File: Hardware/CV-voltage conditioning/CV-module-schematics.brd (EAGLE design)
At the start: 72.4 x 100 mm, 62 parts, among them IC2 LM358D, IC3 LM358D, IC4 LM358D, IC5 LM358D

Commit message: updates
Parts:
- added JP3: (no value), pinhead:1X03
- moved JP2 169.2 mm to (17.8, 92.7), turned to 90 degrees
- moved JP1 83.5 mm to (20.3, 14.0), turned to 180 degrees
- moved C7 81.2 mm to (16.5, 22.9), flipped to the bottom
- moved C3 80.8 mm to (-8.89, 38.1)
- moved C8 80.7 mm to (12.7, 19.1)
- moved C4 76.9 mm to (-7.62, 30.5)
- moved C5 66.5 mm to (29.2, 11.4)
- moved C1 59.5 mm to (-8.89, 24.1)
- moved C6 58.5 mm to (15.2, 3.81), flipped to the bottom, turned to 90 degrees
- moved R7 48.7 mm to (17.7, 19.6), flipped to the bottom, turned to 90 degrees
- moved C2 47.9 mm to (27.9, 2.54), flipped to the bottom, turned to 270 degrees
- moved R5 42.6 mm to (20.4, 19.6), flipped to the bottom, turned to 90 degrees
- moved R8 41.0 mm to (17.8, 7.62), turned to 270 degrees
- moved R3 37.1 mm to (22.8, 19.7), flipped to the bottom, turned to 90 degrees
- moved R6 35.3 mm to (20.3, 7.62), flipped to the bottom, turned to 270 degrees
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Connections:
- net +12VDC: now also JP3.1
- net -12VDC: now also JP3.3
- net GND: now also JP3.2
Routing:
- net N$28: track 0.00 -> 105.0 mm, vias 0 -> 1
- net N$32: track 0.00 -> 82.4 mm, vias 0 -> 1
- net N$1: track 0.00 -> 72.4 mm, vias 0 -> 1
- net N$3: track 0.00 -> 71.1 mm
- net N$30: track 0.00 -> 68.8 mm
- net N$2: track 0.00 -> 67.3 mm
- net N$31: track 0.00 -> 59.5 mm, vias 0 -> 2
- net N$29: track 0.00 -> 34.1 mm, vias 0 -> 2
- net +5V: track 192.0 -> 183.0 mm
- net -12VDC: track 160.7 -> 168.9 mm
- net GND: track 193.3 -> 200.2 mm, vias 5 -> 4
- net +12VDC: track 211.6 -> 216.8 mm
- net VDAC4: track 0.00 -> 4.27 mm
- net VDAC8: track 0.00 -> 4.23 mm
- net VDAC6: track 0.00 -> 4.23 mm
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
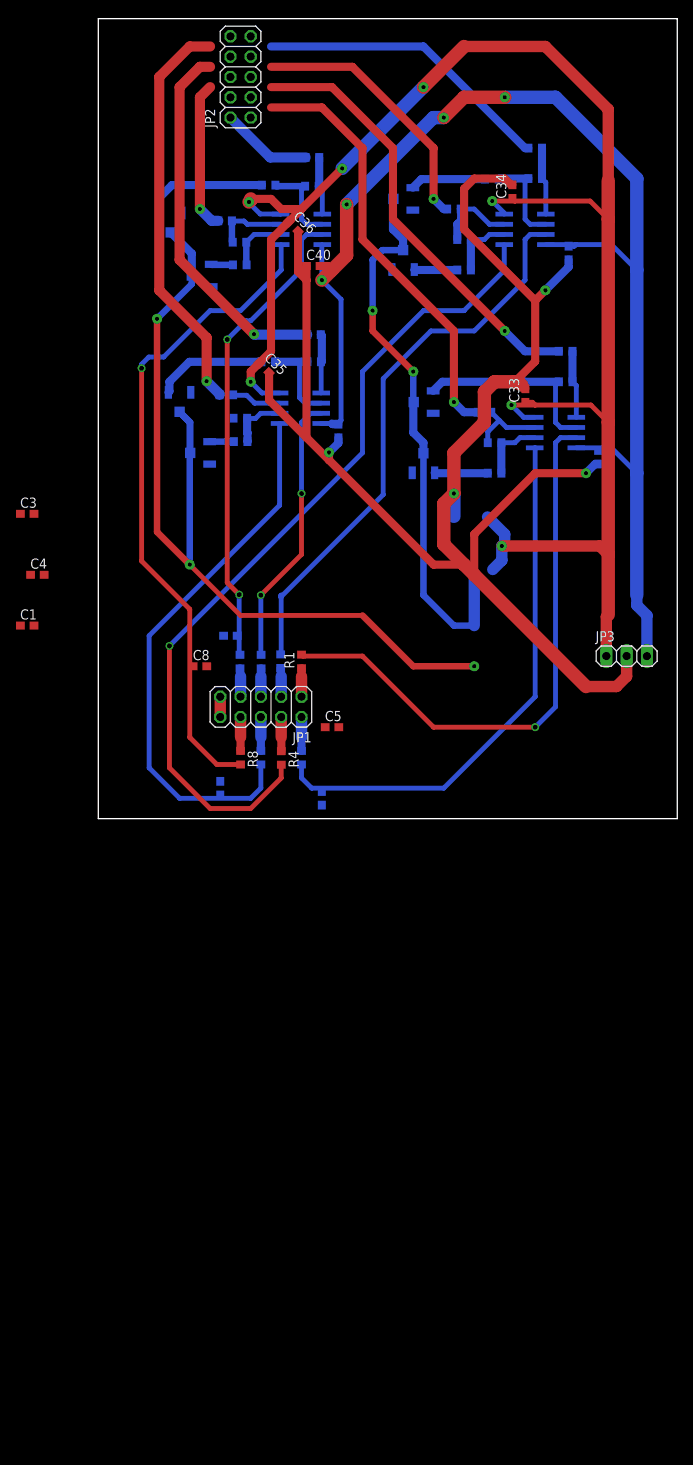
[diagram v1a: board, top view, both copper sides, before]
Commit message: updates for voltage-level module
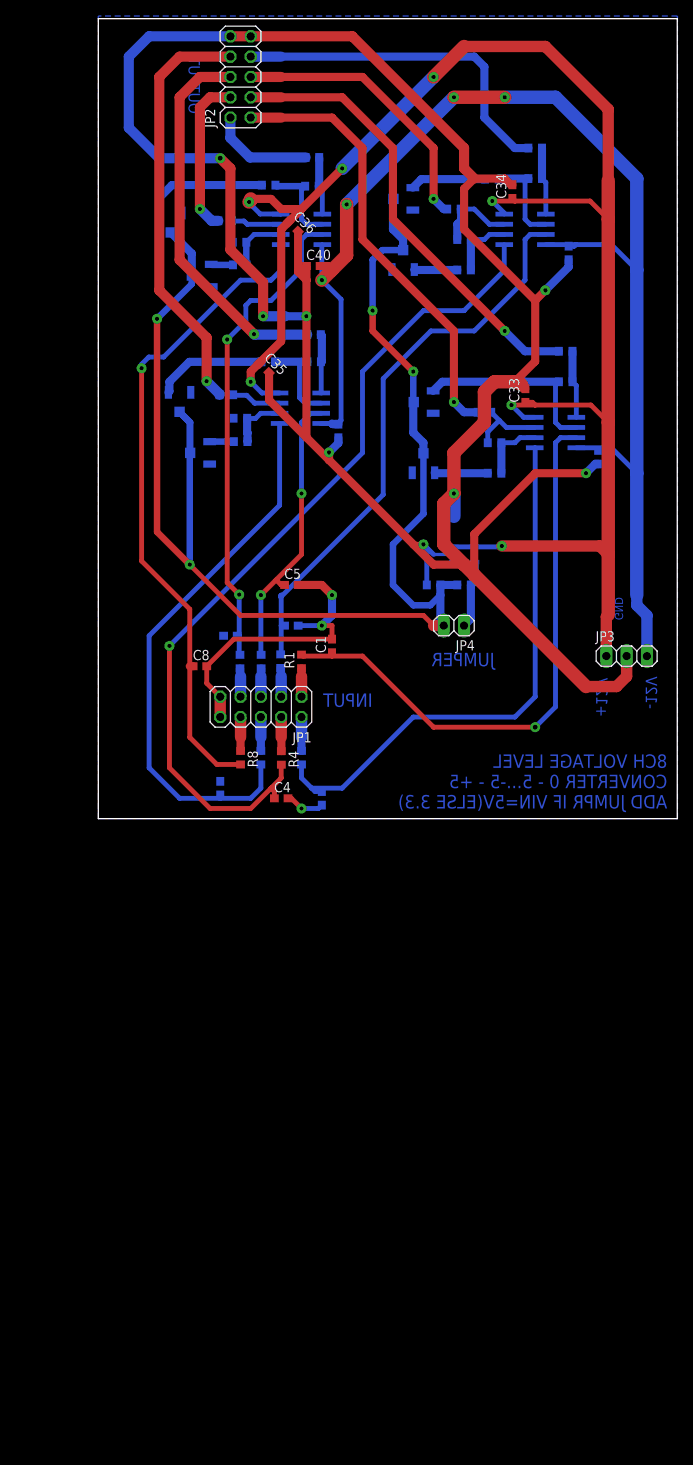
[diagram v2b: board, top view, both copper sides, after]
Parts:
- added JP4: (no value), pinhead:1X02
- added LM4120: LM4120, Pekkas_libraries:SOT23-5
- added R10: 39k, resistor:R0603
- added R9: 20k, resistor:R0603
- moved C4 41.3 mm to (22.9, 2.54)
- moved C1 38.2 mm to (29.2, 21.6), turned to 90 degrees
- moved C3 35.9 mm to (24.1, 24.1), flipped to the bottom, turned to 180 degrees
- moved C5 18.5 mm to (24.1, 29.2)
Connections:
- new net N$34: JP4.1, LM4120.5, R9.2
- net +12VDC: now also LM4120.3, LM4120.4
- net +5V: now also JP4.2, R10.2, R9.1
- net GND: now also LM4120.2, R10.1
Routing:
- net GND: track 200.2 -> 355.2 mm, vias 4 -> 11
- net N$34: track 0.00 -> 8.48 mm
- net CV4: track 37.4 -> 43.2 mm
- net +5V: track 183.0 -> 177.4 mm, vias 5 -> 4
- net +12VDC: track 216.8 -> 214.8 mm
- net CV8: track 50.8 -> 52.8 mm
- net CV2: track 54.9 -> 56.9 mm
- net CV3: track 33.1 -> 35.1 mm
- net CV1: track 53.5 -> 55.5 mm
- net CV5: track 11.5 -> 13.0 mm
- net N$2: track 67.3 -> 68.8 mm
- net N$28: track 105.0 -> 106.5 mm
- net N$31: track 59.5 -> 60.9 mm
- net N$29: track 34.1 -> 35.4 mm
- net CV6: track 18.7 -> 19.9 mm
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- added copper zone on layer 16, net GND
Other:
- board text added: "+12V"
- board text added: "-12V"
- board text added: "8CH VOLTAGE LEVEL"
- board text added: "ADD JUMPR IF VIN=5V(ELSE 3.3)"
- board text added: "CONVERTER 0 - 5...-5 - +5"
- board text added: "GND"
- board text added: "INPUT"
- board text added: "JUMPER"
- board text added: "OUTPUT"

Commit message: layouts
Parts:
- R28, R29, R30, R31, R32, R33, R34, R35: device pot:3223W -> Pekkas_libraries:3222W
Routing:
- net +5V: track 177.4 -> 178.5 mm
- net GND: track 355.2 -> 354.4 mm
- added copper zone on layer 1, net GND
